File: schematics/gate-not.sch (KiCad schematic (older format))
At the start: 3 parts, among them Q13 NPN

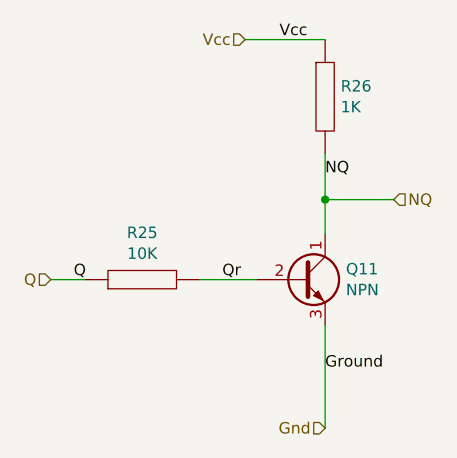
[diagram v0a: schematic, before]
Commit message: Fleshes out basic schematics and some utility software
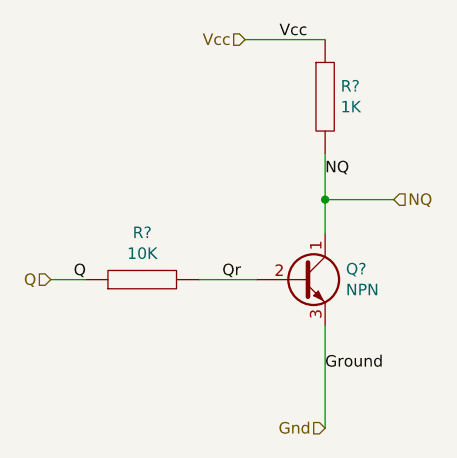
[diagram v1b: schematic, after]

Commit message: Adds ALU Schematics (#1)
* Adds a test for the 4-4-1 multiplexer
* Adds an xor gate
* Updates gitignore to include common swap files and data output
* Adds a four bit bitwise inverter
* Adds a one bit buffer
* Adds a 1->4 bit replicator
* Adds a 4 bit and gate
* ALU is sketched but has functional defects
* Adds a netlist "optimizer" which shortens names for better output parsing
* Adds a simple spice runner
* Adds a model injector and an op test injector
* Basic unit test automation framework for async circuits
* Adds a primitive directory iterator
* Adds some tests for and-2, nor-2, nor-3
* More testing.  Trying to find defect in ALU
* ALU appears to work as expected
* Updates README, adds some ALU tests
* Updates the schematics' README
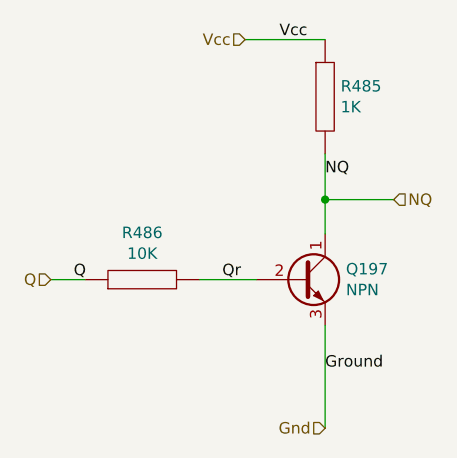
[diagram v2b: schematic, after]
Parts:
- removed Q13: NPN, Package_TO_SOT_THT:TO-92_Inline, symbol Transistor_BJT:BC548
- removed R37: 10K, symbol pspice:R
- removed R38: 1K, symbol pspice:R
- added Q41: NPN, Package_TO_SOT_THT:TO-92_Inline, symbol Transistor_BJT:BC548
- added R97: 1K, symbol pspice:R
- added R98: 10K, symbol pspice:R
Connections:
- net Gnd: now also Q41.3 (E)
- net NQ: now also Q41.1 (C), R97.2
- net Q: now also R98.1
- net Qr: now also Q41.2 (B), R98.2
- net Vcc: now also R97.1
